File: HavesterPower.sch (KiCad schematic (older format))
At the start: 41 parts, among them U6 ADP5091ACPZ-1-R7, U7 LT3009IDCTRMPBF, U8 LT3009IDCTRMPBF

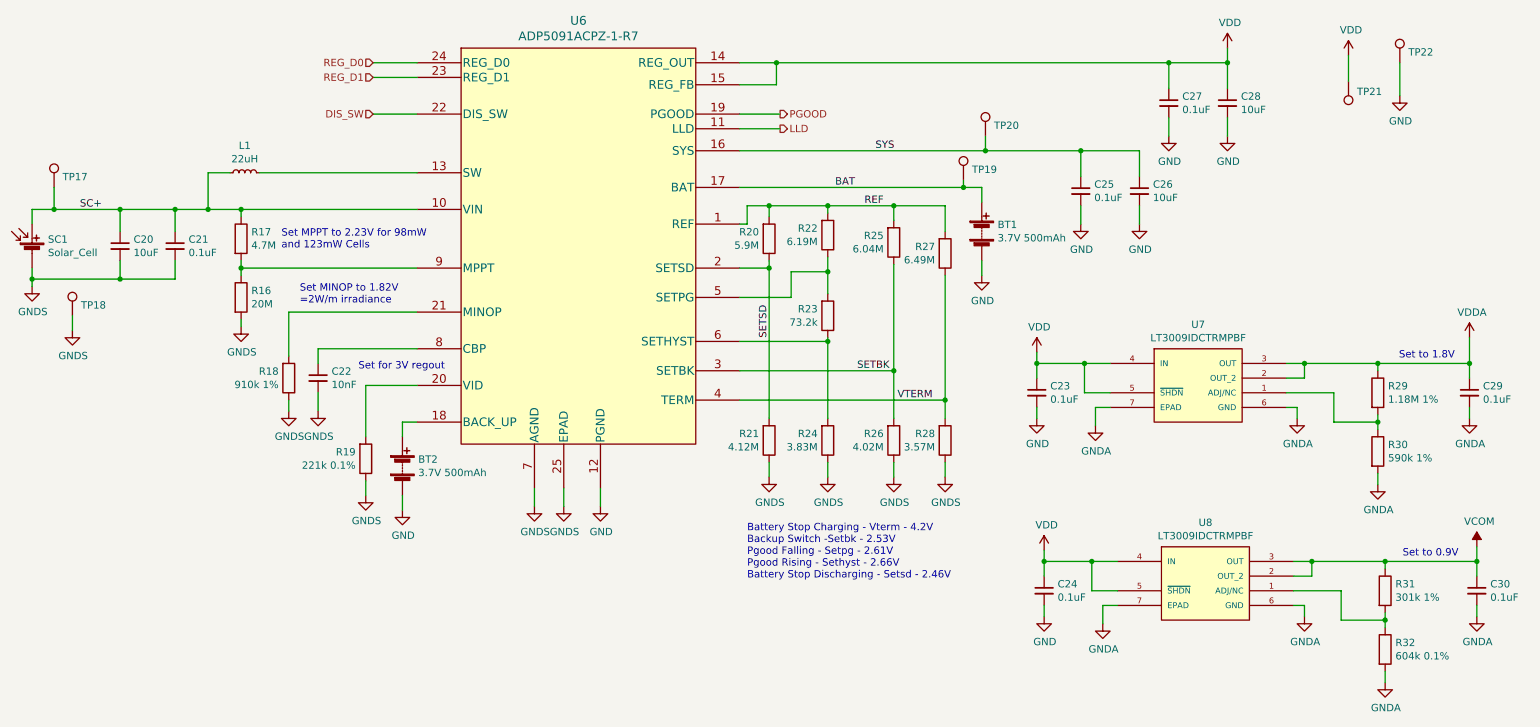
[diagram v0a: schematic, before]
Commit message: redid power section with new energy harverster ic
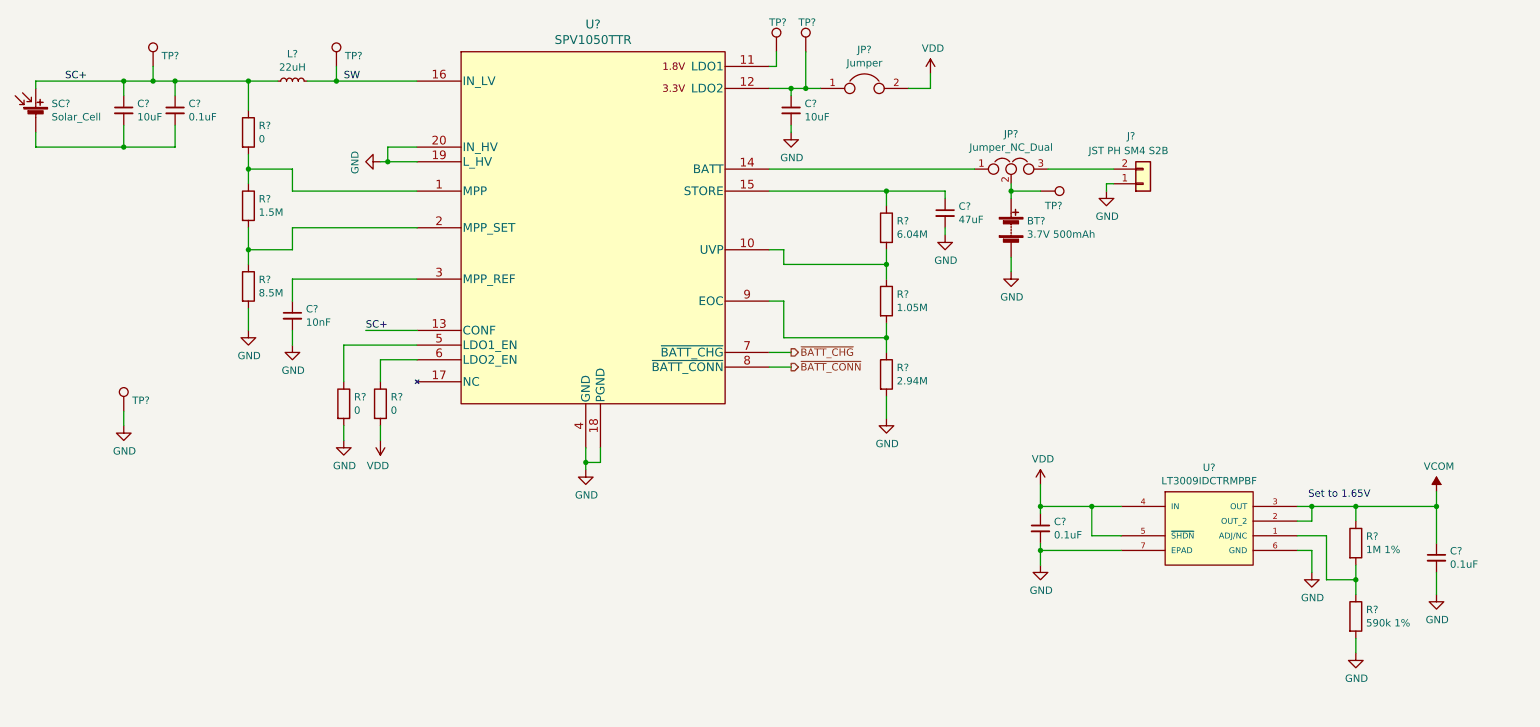
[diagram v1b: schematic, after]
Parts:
- removed BT2: 3.7V 500mAh, PatchV2:RJD-ST1, symbol Device:Battery
- removed C23, C25, C27, C29: 0.1uF, Capacitor_SMD:C_0402_1005Metric, symbol Device:C_Small
- removed C26, C28: 10uF, Capacitor_SMD:C_0402_1005Metric, symbol Device:C_Small
- removed R16: 20M, Resistor_SMD:R_0603_1608Metric, symbol Device:R
- removed R17: 4.7M, Resistor_SMD:R_0603_1608Metric, symbol Device:R
- removed R18: 910k 1%, Resistor_SMD:R_0402_1005Metric, symbol Device:R
- removed R19: 221k 0.1%, Resistor_SMD:R_0402_1005Metric, symbol Device:R
- removed R20: 5.9M, Resistor_SMD:R_0603_1608Metric, symbol Device:R
- removed R21: 4.12M, Resistor_SMD:R_0402_1005Metric, symbol Device:R
- removed R22: 6.19M, Resistor_SMD:R_0603_1608Metric, symbol Device:R
- removed R23: 73.2k, Resistor_SMD:R_0402_1005Metric, symbol Device:R
- removed R24: 3.83M, Resistor_SMD:R_0402_1005Metric, symbol Device:R
- removed R25: 6.04M, Resistor_SMD:R_0402_1005Metric, symbol Device:R
- removed R26: 4.02M, Resistor_SMD:R_0402_1005Metric, symbol Device:R
- removed R27: 6.49M, Resistor_SMD:R_0402_1005Metric, symbol Device:R
- removed R28: 3.57M, Resistor_SMD:R_0402_1005Metric, symbol Device:R
- removed R31: 301k 1%, Resistor_SMD:R_0402_1005Metric, symbol Device:R
- removed R32: 604k 0.1%, Resistor_SMD:R_0402_1005Metric, symbol Device:R
- removed TP19, TP20: TestPoint, TestPoint:TestPoint_Pad_1.5x1.5mm, symbol Connector:TestPoint
- removed U6: ADP5091ACPZ-1-R7, PatchV2:ADP5091ACPZ-1-R7, symbol PatchV2:ADP5091ACPZ-1-R7
- removed U7: LT3009IDCTRMPBF, PatchV2:DFN-6_DC, symbol PatchV2:LT3009IDCTRMPBF
- added C?: 47uF, Capacitor_SMD:C_0805_2012Metric, symbol Device:C_Small
- added C?: 10uF, Capacitor_SMD:C_0402_1005Metric, symbol Device:C_Small
- added J?: JST PH SM4 S2B, PatchV2:JST-S2B-PH-SM4-TBLFSN-Manufacturer_Recommended, symbol Connector_Generic:Conn_01x02
- added JP?: Jumper_NC_Dual, symbol Device:Jumper_NC_Dual
- added JP?: Jumper, symbol Device:Jumper
- added R? (x3): 0, Resistor_SMD:R_0402_1005Metric, symbol Device:R
- added R?: 1.5M, Resistor_SMD:R_0603_1608Metric, symbol Device:R
- added R?: 8.5M, Resistor_SMD:R_0603_1608Metric, symbol Device:R
- added R?: 6.04M, Resistor_SMD:R_0402_1005Metric, symbol Device:R
- added R?: 1.05M, Resistor_SMD:R_0603_1608Metric, symbol Device:R
- added R?: 2.94M, Resistor_SMD:R_0402_1005Metric, symbol Device:R
- added TP? (x2): TestPoint, TestPoint:TestPoint_Pad_1.5x1.5mm, symbol Connector:TestPoint
- added U?: SPV1050TTR, PatchV2:SPV1050TTR, symbol PatchV2:SPV1050TTR
- C?: renamed from C20; DigiKey_PN (none) -> 2679-C0402X5R6R3-106MNP-CT-ND
- R?: renamed from R29; value 1.18M 1% -> 1M 1%; Digi-Key_PN 541-1.18MLCT-ND -> P1.00MLCT-ND
- renumbered BT1 to BT?, C30 to C?, C24 to C?, C21 to C?, C22 to C?, L1 to L?, R30 to R?, SC1 to SC?, TP17 to TP?, TP18 to TP?, TP22 to TP?, TP21 to TP?, U8 to U?
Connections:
- net GNDA is gone; now on net GND: C?.2, R?.2, U?.6 (GND), U?.7 (EPAD)
- net VDDA is gone; now on net VCOM: R?.1
- net GND: now also C?.2, TP?.1, C?.2, C?.2, J?.1 (Pin_1), R?.2, R?.2, R?.2, U?.18 (PGND), U?.19 (L_HV), U?.20 (IN_HV), U?.4 (GND); no longer TP?.1
- net SC+: now also R?.1, U?.13 (CONF)
- net VDD: now also JP?.2, R?.2; no longer TP?.1
- net SW: now reaches L?.2
- net SW: now also TP?.1, U?.16 (IN_LV)
- net at C?.1: now also U?.3 (MPP_REF)
- net at U?.1 (ADJ/NC): now also R?.1, R?.2
- net BAT: no longer names the net of BT?.1 (+)
- net BAT: now also TP?.1, JP?.2
- net GNDS: no longer names the net of C?.2, C?.2, SC?.2 (-)
- net GNDS: no longer C?.2, TP?.1
- new net: TP?.1, U?.11 (LDO1)
- new net: R?.1, R?.2, U?.1 (MPP)
- new net: R?.1, R?.2, U?.10 (UVP)
- new net: C?.1, JP?.1, TP?.1, U?.12 (LDO2)
- new net: JP?.1, U?.14 (BATT)
- new net: C?.1, R?.1, U?.15 (STORE)
- new net: R?.1, R?.2, U?.2 (MPP_SET)
- new net: R?.1, U?.5 (LDO1_EN)
- new net: R?.1, U?.6 (LDO2_EN)
- new net: R?.1, R?.2, U?.9 (EOC)
- new net: J?.2 (Pin_2), JP?.3
- new net ~BATT_CHG: U?.7 (~BATT_CHG)
- new net ~BATT_CONN: U?.8 (~BATT_CONN)
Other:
- note added: "Set to 1.65V"
- note removed: "Battery Stop Charging - Vterm - 4.2V\nBackup Switch -Setbk - 2.53V\nPgood Falling - Setpg - 2.61V\nPgood Rising - Sethyst - 2.66V\nBattery Stop Discharging - Setsd - 2.46V\n"
- note removed: "Set MINOP to 1.82V\n=2W/m irradiance"
- note removed: "Set MPPT to 2.23V for 98mW\nand 123mW Cells"
- note removed: "Set for 3V regout"
- note removed: "Set to 0.9V"
- note removed: "Set to 1.8V\n"
- moved on the sheet: BT?, C?, L?, R?, SC?, TP?, U?

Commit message: catch up
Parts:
- JP?: footprint (none) -> Connector_PinHeader_2.54mm:PinHeader_1x03_P2.54mm_Vertical
- JP?: footprint (none) -> Connector_PinHeader_2.54mm:PinHeader_1x02_P2.54mm_Vertical
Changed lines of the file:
@@
 F 0 "JP?" H 7350 2839 50  0000 C CNN
 F 1 "Jumper_NC_Dual" H 7350 2748 50  0000 C CNN
-F 2 "" H 7350 2600 50  0001 C CNN
+F 2 "Connector_PinHeader_2.54mm:PinHeader_1x03_P2.54mm_Vertical" H 7350 2600 50  0001 C CNN
 F 3 "~" H 7350 2600 50  0001 C CNN
 	1    7350 2600
@@
 F 0 "JP?" H 6350 2314 50  0000 C CNN
 F 1 "Jumper" H 6350 2223 50  0000 C CNN
-F 2 "" H 6350 2050 50  0001 C CNN
+F 2 "Connector_PinHeader_2.54mm:PinHeader_1x02_P2.54mm_Vertical" H 6350 2050 50  0001 C CNN
 F 3 "~" H 6350 2050 50  0001 C CNN
 	1    6350 2050

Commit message: schematic functionally finished working on layout
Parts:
- removed R?: 0, Resistor_SMD:R_0402_1005Metric, symbol Device:R
- removed TP?: TestPoint, TestPoint:TestPoint_Pad_1.5x1.5mm, symbol Connector:TestPoint
- added C17: 0.1uF, Capacitor_SMD:C_0402_1005Metric, symbol Device:C_Small
- added R23: 1M 1%, Resistor_SMD:R_0402_1005Metric, symbol Device:R
- added R24, R25: 10M, Resistor_SMD:R_0402_1005Metric, symbol Device:R
- added TP12: TestPoint, TestPoint:TestPoint_Pad_1.5x1.5mm, symbol Connector:TestPoint
- gave numbers to parts that had none: 29
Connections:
- net GND: now also C16.2, C19.2, SC1.2 (-), C17.2
- net SC+: now also C17.1; no longer C19.1
- net ~BATT_CHG: now also R25.2
- net ~BATT_CONN: now also R24.2
- net BATT: now reaches JP2.1, U5.14 (BATT)
- net STORE: now reaches C21.1, R26.1, U5.15 (STORE)
- net STORE: now also R23.2, R24.1, R25.1, TP12.1
- net LDO_3V3_EN: now reaches U5.6 (LDO2_EN)
- net LDO_3V3_EN: now also C19.1, R23.1
- net BATT_CHG: now reaches J7.2 (Pin_2), JP2.3
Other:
- moved on the sheet: C19, R22

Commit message: Finished pre-review layout
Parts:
- R19: value 0 -> 10M; footprint Resistor_SMD:R_0402_1005Metric -> Resistor_SMD:R_0603_1608Metric; Digi-Key_PN 541-2877-1-ND -> 10-ERJ-U03J106VCT-ND
- R20: value 1.5M -> 909k; Digi-Key_PN 311-1.50MHRCT-ND -> 2019-RK73H1JTTD9093FCT-ND
- R21: value 8.5M -> 3.83M; Digi-Key_PN RMCF0603FT8M45CT-ND -> 541-3.83MHCT-ND
- SC1: footprint PatchV2:SM141K04LV -> PatchV2:SM141K10LV
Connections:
- net GND: no longer U5.19 (L_HV), U5.20 (IN_HV)
- net SC+: now also U5.20 (IN_HV); no longer L1.1
- new net: L1.1, U5.19 (L_HV)
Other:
- moved on the sheet: L1, TP9
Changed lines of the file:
@@
 F 0 "SC1" H 808 2346 50  0000 L CNN
 F 1 "Solar_Cell" H 808 2255 50  0000 L CNN
-F 2 "PatchV2:SM141K04LV" V 700 2310 50  0001 C CNN
-F 3 "~" V 700 2310 50  0001 C CNN
+F 2 "PatchV2:SM141K10LV" V 700 2310 50  0001 C CNN
+F 3 "https://waf-e.dubudisk.com/anysolar.dubuplus.com/techsupport@anysolar.biz/O18Ae0F/DubuDisk/www/Gen3/SM141K10LV%20DATA%20SHEET%20202007.pdf" V 700 2310 50  0001 C CNN
 F 4 "SM141K04LV" H 700 2250 50  0001 C CNN "Digi-Key_PN"
 	1    700  2250
@@
 L Device:L_Small L1
 U 1 1 605DC9E2
-P 2450 2000
-F 0 "L1" V 2635 2000 50  0000 C CNN
-F 1 "22uH" V 2544 2000 50  0000 C CNN
-F 2 "PatchV2:WE-LHMI_4020" H 2450 2000 50  0001 C CNN
-F 3 "~" H 2450 2000 50  0001 C CNN
-F 4 "732-3340-1-ND" V 2450 2000 50  0001 C CNN "Digi-Key_PN"
-	1    2450 2000
-	0    -1   -1   0
+P 2825 2150
+F 0 "L1" V 3010 2150 50  0000 C CNN
+F 1 "22uH" V 2919 2150 50  0000 C CNN
+F 2 "PatchV2:WE-LHMI_4020" H 2825 2150 50  0001 C CNN
+F 3 "~" H 2825 2150 50  0001 C CNN
+F 4 "732-3340-1-ND" V 2825 2150 50  0001 C CNN "Digi-Key_PN"
+	1    2825 2150
+	-1   0    0    1
 $EndComp
 $Comp
@@
 	1300 2450 1650 2450
 Wire Wire Line
-	2550 2000 2750 2000
-Wire Wire Line
-	3300 2550 3100 2550
-Wire Wire Line
-	3100 2550 3100 2450
-Wire Wire Line
-	3100 2450 3300 2450
-$Comp
-L power:GND #PWR0151
-U 1 1 611F8729
-P 3050 2550
-F 0 "#PWR0151" H 3050 2300 50  0001 C CNN
-F 1 "GND" H 3055 2377 50  0000 C CNN
-F 2 "" H 3050 2550 50  0001 C CNN
-F 3 "" H 3050 2550 50  0001 C CNN
-	1    3050 2550
-	0    1    1    0
-$EndComp
-Wire Wire Line
-	3050 2550 3100 2550
-Connection ~ 3100 2550
-Wire Wire Line
 	1500 1900 1500 2000
 Connection ~ 1500 2000
@@
 L Connector:TestPoint TP?
 U 1 1 61208AAE
-P 2750 1900
+P 2825 1900
 AR Path="/61208AAE" Ref="TP?"  Part="1"
 AR Path="/605A6F24/61208AAE" Ref="TP9"  Part="1"
-F 0 "TP9" H 2808 1972 50  0000 L CNN
-F 1 "TestPoint" H 2808 1927 50  0001 L CNN
-F 2 "TestPoint:TestPoint_Pad_1.5x1.5mm" H 2950 1900 50  0001 C CNN
-F 3 "~" H 2950 1900 50  0001 C CNN
-	1    2750 1900
-	1    0    0    -1
-$EndComp
-Wire Wire Line
-	2750 1900 2750 2000
-Connection ~ 2750 2000
+F 0 "TP9" H 2883 1972 50  0000 L CNN
+F 1 "TestPoint" H 2883 1927 50  0001 L CNN
+F 2 "TestPoint:TestPoint_Pad_1.5x1.5mm" H 3025 1900 50  0001 C CNN
+F 3 "~" H 3025 1900 50  0001 C CNN
+	1    2825 1900
+	1    0    0    -1
+$EndComp
 Text Label 900  2000 0    50   ~ 0
 SC+
-Text Label 2800 2000 0    50   ~ 0
+Text Label 3050 2000 0    50   ~ 0
 SW
 $Comp
@@
 P 2150 2350
 F 0 "R19" H 2220 2396 50  0000 L CNN
-F 1 "0" H 2220 2305 50  0000 L CNN
-F 2 "Resistor_SMD:R_0402_1005Metric" V 2080 2350 50  0001 C CNN
+F 1 "10M" H 2220 2305 50  0000 L CNN
+F 2 "Resistor_SMD:R_0603_1608Metric" V 2080 2350 50  0001 C CNN
 F 3 "~" H 2150 2350 50  0001 C CNN
-F 4 "541-2877-1-ND" H 2150 2350 50  0001 C CNN "Digi-Key_PN"
+F 4 "10-ERJ-U03J106VCT-ND" H 2150 2350 50  0001 C CNN "Digi-Key_PN"
 	1    2150 2350
 	1    0    0    -1
@@
 P 2150 2850
 F 0 "R20" H 2220 2896 50  0000 L CNN
-F 1 "1.5M" H 2220 2805 50  0000 L CNN
+F 1 "909k" H 2220 2805 50  0000 L CNN
 F 2 "Resistor_SMD:R_0603_1608Metric" V 2080 2850 50  0001 C CNN
 F 3 "~" H 2150 2850 50  0001 C CNN
-F 4 "311-1.50MHRCT-ND" H 2150 2850 50  0001 C CNN "Digi-Key_PN"
+F 4 "2019-RK73H1JTTD9093FCT-ND" H 2150 2850 50  0001 C CNN "Digi-Key_PN"
 	1    2150 2850
 	1    0    0    -1
@@
 P 2150 3400
 F 0 "R21" H 2220 3446 50  0000 L CNN
-F 1 "8.5M" H 2220 3355 50  0000 L CNN
+F 1 "3.83M" H 2220 3355 50  0000 L CNN
 F 2 "Resistor_SMD:R_0603_1608Metric" V 2080 3400 50  0001 C CNN
 F 3 "~" H 2150 3400 50  0001 C CNN
-F 4 "RMCF0603FT8M45CT-ND" H 2150 3400 50  0001 C CNN "Digi-Key_PN"
+F 4 "541-3.83MHCT-ND" H 2150 3400 50  0001 C CNN "Digi-Key_PN"
 	1    2150 3400
 	1    0    0    -1
@@
 	2150 3550 2150 3700
 Wire Wire Line
-	2150 2000 2350 2000
-Wire Wire Line
 	2150 3150 2450 3150
 Wire Wire Line
@@
 Text Label 2950 3700 0    50   ~ 0
 SC+
-Wire Wire Line
-	2750 2000 3300 2000
 Wire Wire Line
 	2450 2750 3300 2750
@@
 Wire Wire Line
 	5850 2050 6050 2050
+Wire Wire Line
+	2475 2000 2475 2450
+Wire Wire Line
+	2475 2450 3300 2450
+Wire Wire Line
+	2150 2000 2475 2000
+Wire Wire Line
+	2825 2050 2825 2000
+Wire Wire Line
+	2825 2250 2825 2550
+Wire Wire Line
+	2825 2550 3300 2550
+Wire Wire Line
+	2825 1900 2825 2000
+Connection ~ 2825 2000
+Wire Wire Line
+	2825 2000 3300 2000
 $EndSCHEMATC
